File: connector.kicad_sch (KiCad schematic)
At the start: 1 part, among them J1 PCIEx4_HOST

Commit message: Finish v1.0
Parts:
- added C6: 100nF, Capacitor_SMD:C_0603_1608Metric, symbol Device:C
- added Q1: MMBT3904, Package_TO_SOT_SMD:SOT-23, symbol Transistor_BJT:MMBT3904
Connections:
- net B30: now reaches J1.B30
- net B30: now also C6.1, Q1.1 (B), Q1.3 (C)
- net B31: now reaches J1.B31
- net B31: now also C6.2, Q1.2 (E)
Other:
- note added: "The Terramaster F2 motherboard has a PCIe x4 connector with non-standard pinout. It provides 12V, 5V and 3.3V power rails, 2xSATA and 2xPCIe (gen 2) 1-lane. The purpose of pins A1, A11, A32, B10, B11, B30 and B31 are unknown to me but leaving them unconnected result in a working backplane. ¯\_(ツ)_/¯"
- note added: "This little circuit was on my existing F2-221's backplane PCB. I added it here just in case but leaving it unpopulated seems to be fine."
- title: (none) -> F3 Backplane Connector
- moved on the sheet: J1

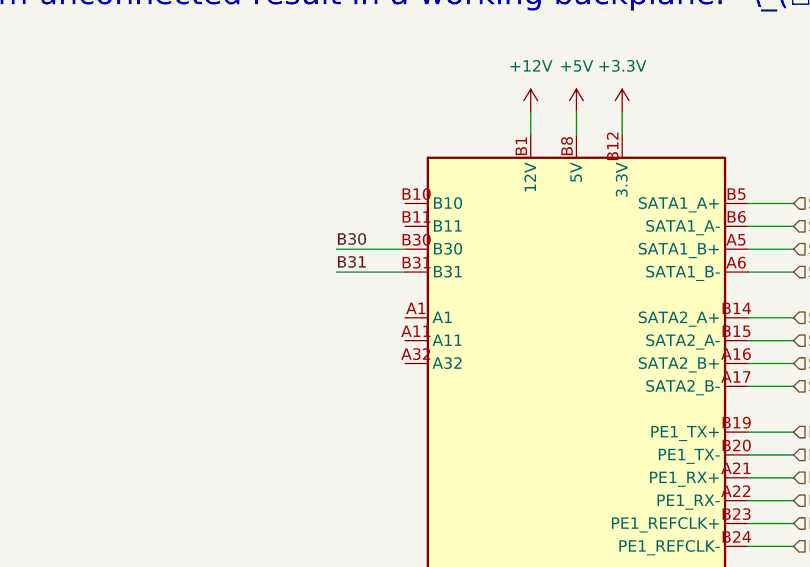
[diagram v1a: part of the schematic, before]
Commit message: Add datasheet links and digikey part numbers
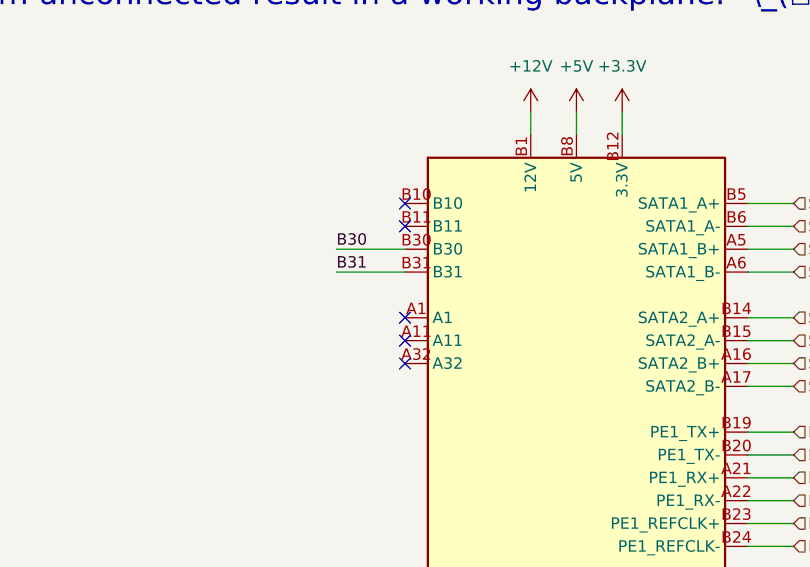
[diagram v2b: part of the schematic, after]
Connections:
- no-connect marks 0 -> 5
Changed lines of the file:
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@@
   (junction (at 257.81 93.98) (diameter 0) (color 0 0 0 0)
   )
+  (no_connect (at 139.7 86.36))
+  (no_connect (at 139.7 73.66))
+  (no_connect (at 139.7 91.44))
+  (no_connect (at 139.7 76.2))
+  (no_connect (at 139.7 88.9))
   (wire (pts (xy 266.7 88.9) (xy 257.81 88.9))
     (stroke (width 0) (type default))

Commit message: Remove edge connector from bill of materials
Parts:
- J1: now left out of the parts list
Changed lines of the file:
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@@
   )
   (symbol (lib_id "Connector_Backplane:PCIEx4_HOST") (at 158.75 86.36 0) (unit 1)
-    (in_bom yes) (on_board yes) (dnp no) (fields_autoplaced)
+    (in_bom no) (on_board yes) (dnp no) (fields_autoplaced)
     (property "Reference" "J1" (at 160.9441 124.46 0)
       (effects (font (size 1.27 1.27)) (justify left))
